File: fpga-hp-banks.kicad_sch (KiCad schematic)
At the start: 9 parts, among them U34 XCAU25P-2FFVB676I

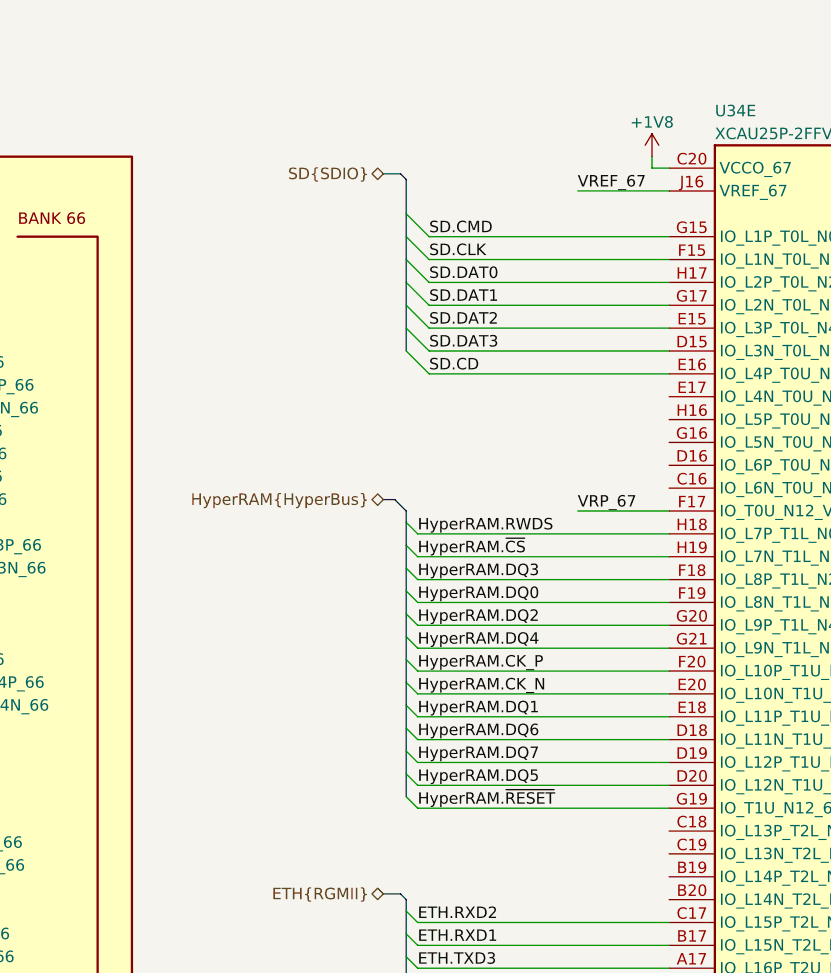
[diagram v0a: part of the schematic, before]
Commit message: [#67016] Remap HyperRAM interface
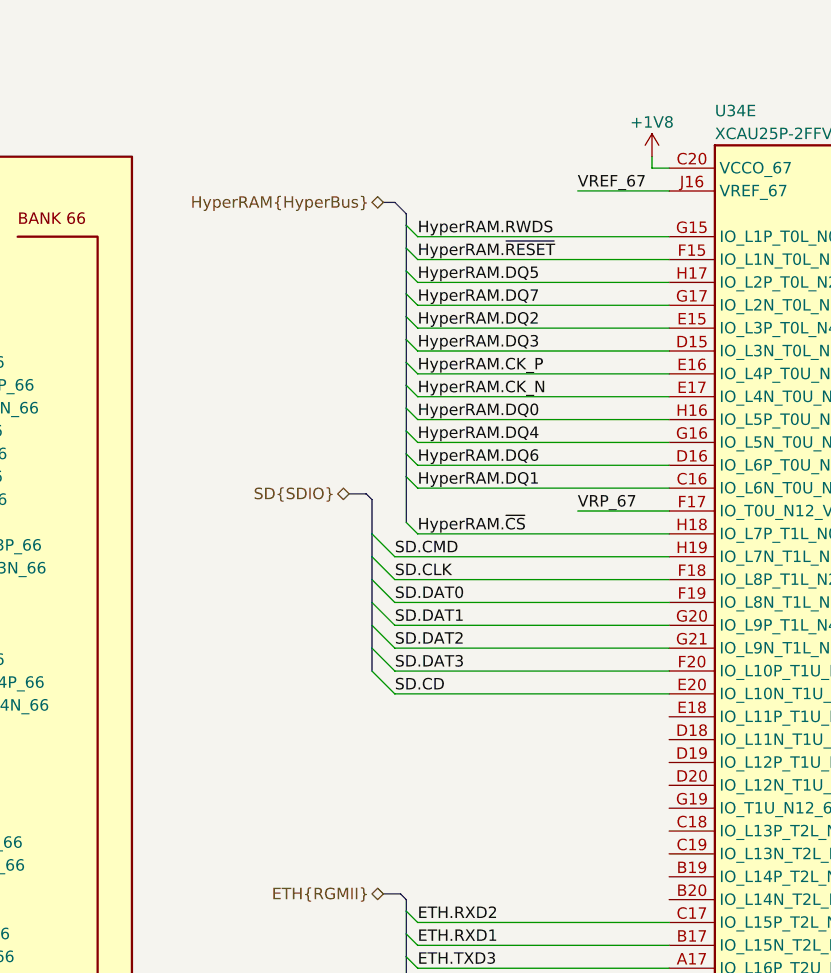
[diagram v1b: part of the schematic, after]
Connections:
- net HyperRAM.CK_N: now also U34.E17 (IO_L4N_T0U_N7_DBC_AD7N_67); no longer U34.E20 (IO_L10N_T1U_N7_QBC_AD4N_67)
- net HyperRAM.CK_P: now also U34.E16 (IO_L4P_T0U_N6_DBC_AD7P_67); no longer U34.F20 (IO_L10P_T1U_N6_QBC_AD4P_67)
- net HyperRAM.DQ0: now also U34.H16 (IO_L5P_T0U_N8_AD14P_67); no longer U34.F19 (IO_L8N_T1L_N3_AD5N_67)
- net HyperRAM.DQ1: now also U34.C16 (IO_L6N_T0U_N11_AD6N_67); no longer U34.E18 (IO_L11P_T1U_N8_GC_67)
- net HyperRAM.DQ2: now also U34.E15 (IO_L3P_T0L_N4_AD15P_67); no longer U34.G20 (IO_L9P_T1L_N4_AD12P_67)
- net HyperRAM.DQ3: now also U34.D15 (IO_L3N_T0L_N5_AD15N_67); no longer U34.F18 (IO_L8P_T1L_N2_AD5P_67)
- net HyperRAM.DQ4: now also U34.G16 (IO_L5N_T0U_N9_AD14N_67); no longer U34.G21 (IO_L9N_T1L_N5_AD12N_67)
- net HyperRAM.DQ5: now also U34.H17 (IO_L2P_T0L_N2_67); no longer U34.D20 (IO_L12N_T1U_N11_GC_67)
- net HyperRAM.DQ6: now also U34.D16 (IO_L6P_T0U_N10_AD6P_67); no longer U34.D18 (IO_L11N_T1U_N9_GC_67)
- net HyperRAM.DQ7: now also U34.G17 (IO_L2N_T0L_N3_67); no longer U34.D19 (IO_L12P_T1U_N10_GC_67)
- net HyperRAM.RWDS: now also U34.G15 (IO_L1P_T0L_N0_DBC_67); no longer U34.H18 (IO_L7P_T1L_N0_QBC_AD13P_67)
- net HyperRAM.~{CS}: now also U34.H18 (IO_L7P_T1L_N0_QBC_AD13P_67); no longer U34.H19 (IO_L7N_T1L_N1_QBC_AD13N_67)
- net HyperRAM.~{RESET}: now also U34.F15 (IO_L1N_T0L_N1_DBC_67); no longer U34.G19 (IO_T1U_N12_67)
- net SD.CD: now also U34.E20 (IO_L10N_T1U_N7_QBC_AD4N_67); no longer U34.E16 (IO_L4P_T0U_N6_DBC_AD7P_67)
- net SD.CLK: now also U34.F18 (IO_L8P_T1L_N2_AD5P_67); no longer U34.F15 (IO_L1N_T0L_N1_DBC_67)
- net SD.CMD: now also U34.H19 (IO_L7N_T1L_N1_QBC_AD13N_67); no longer U34.G15 (IO_L1P_T0L_N0_DBC_67)
- net SD.DAT0: now also U34.F19 (IO_L8N_T1L_N3_AD5N_67); no longer U34.H17 (IO_L2P_T0L_N2_67)
- net SD.DAT1: now also U34.G20 (IO_L9P_T1L_N4_AD12P_67); no longer U34.G17 (IO_L2N_T0L_N3_67)
- net SD.DAT2: now also U34.G21 (IO_L9N_T1L_N5_AD12N_67); no longer U34.E15 (IO_L3P_T0L_N4_AD15P_67)
- net SD.DAT3: now also U34.F20 (IO_L10P_T1U_N6_QBC_AD4P_67); no longer U34.D15 (IO_L3N_T0L_N5_AD15N_67)

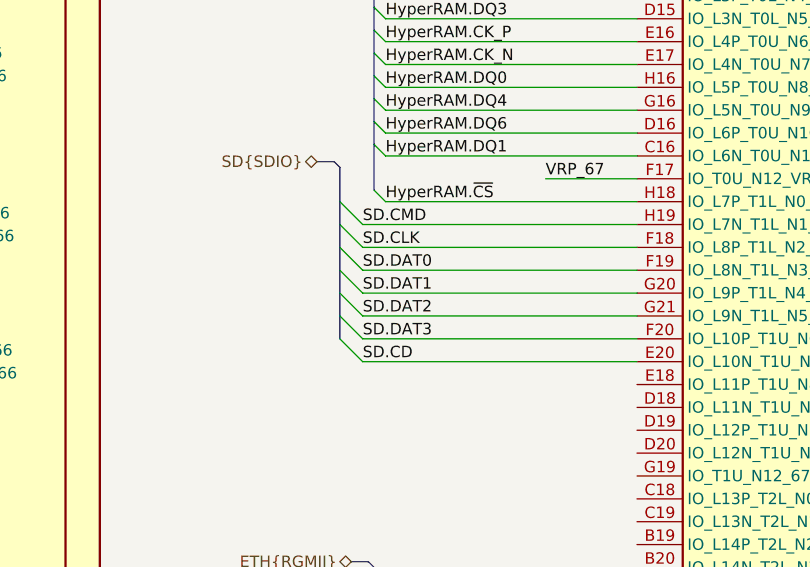
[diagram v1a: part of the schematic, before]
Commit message: [#67016] Connect SD card
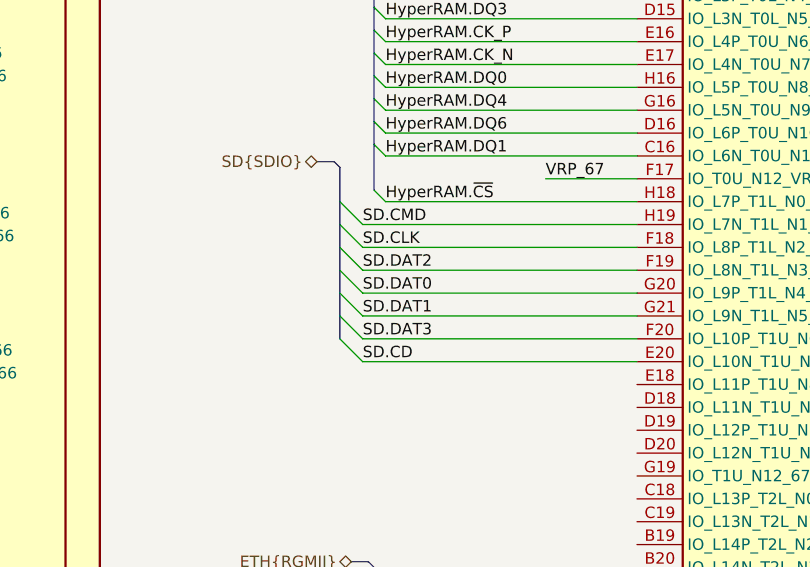
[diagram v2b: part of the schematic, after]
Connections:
- net SD.DAT0: now also U34.G20 (IO_L9P_T1L_N4_AD12P_67); no longer U34.F19 (IO_L8N_T1L_N3_AD5N_67)
- net SD.DAT1: now also U34.G21 (IO_L9N_T1L_N5_AD12N_67); no longer U34.G20 (IO_L9P_T1L_N4_AD12P_67)
- net SD.DAT2: now also U34.F19 (IO_L8N_T1L_N3_AD5N_67); no longer U34.G21 (IO_L9N_T1L_N5_AD12N_67)
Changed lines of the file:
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@@
     (effects (font (size 1.27 1.27)) (justify left bottom))
   )
-  (label "SD.DAT2" (at 311.15 104.14 0) (fields_autoplaced)
+  (label "SD.DAT2" (at 311.15 99.06 0) (fields_autoplaced)
     (effects (font (size 1.27 1.27)) (justify left bottom))
   )
@@
     (effects (font (size 1.27 1.27)) (justify left bottom))
   )
-  (label "SD.DAT1" (at 311.15 101.6 0) (fields_autoplaced)
+  (label "SD.DAT1" (at 311.15 104.14 0) (fields_autoplaced)
     (effects (font (size 1.27 1.27)) (justify left bottom))
   )
@@
     (effects (font (size 1.27 1.27)) (justify left bottom))
   )
-  (label "SD.DAT0" (at 311.15 99.06 0) (fields_autoplaced)
-    (effects (font (size 1.27 1.27)) (justify left bottom))
-  )
+  (label "SD.DAT0" (at 311.15 101.6 0) (fields_autoplaced)
+    (effects (font (size 1.27 1.27)) (justify left bottom))
+  )

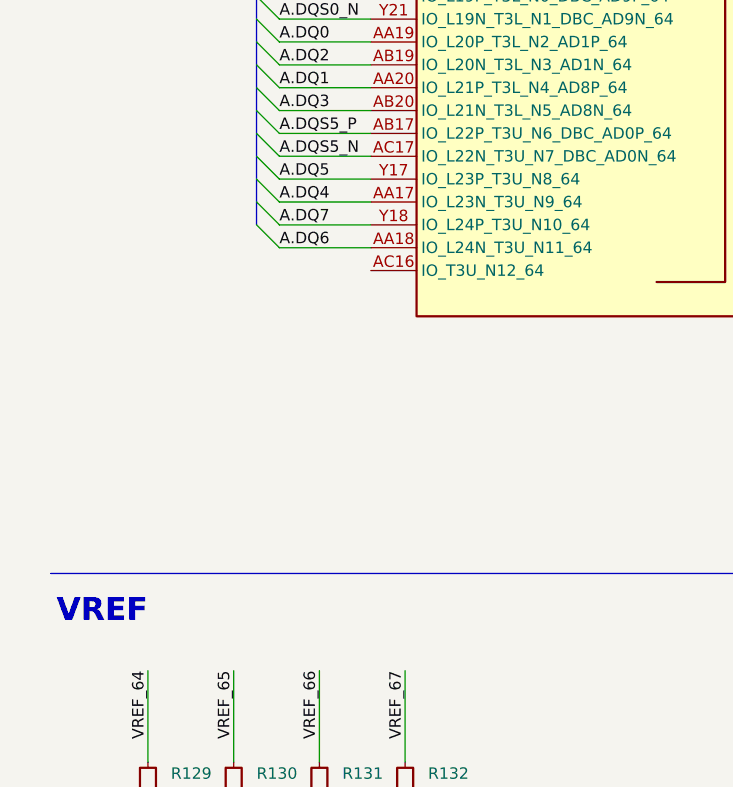
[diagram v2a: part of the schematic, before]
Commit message: [#67115] Place decoupling under FPGA
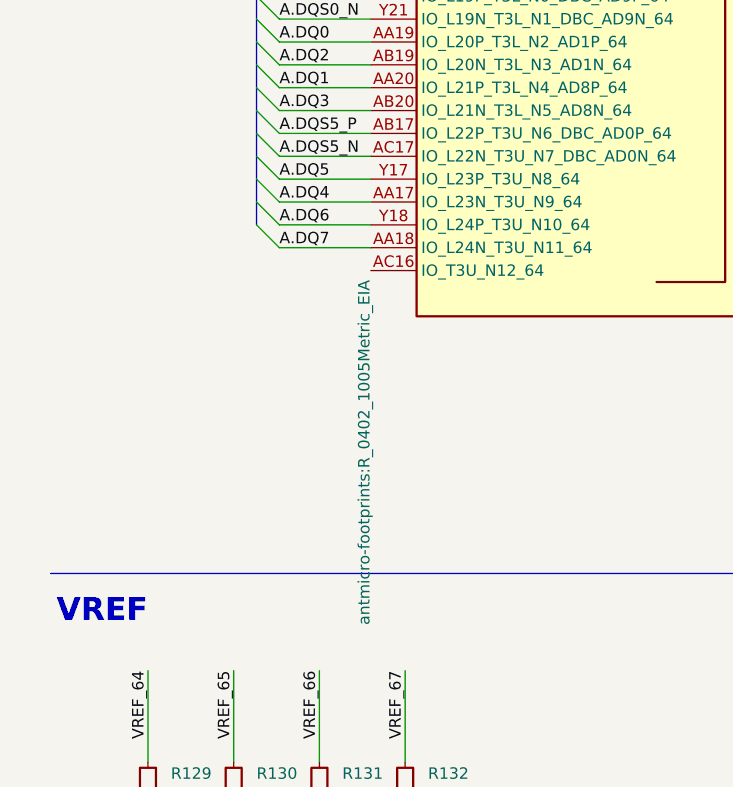
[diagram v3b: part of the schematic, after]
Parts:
- R129, R130, R131, R132, R133, R134, R180, R182: footprint antmicro-footprints:R_0402_1005Metric -> antmicro-footprints:R_0402_1005Metric_EIA
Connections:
- net A.DQ6: now also U34.Y18 (IO_L24P_T3U_N10_64); no longer U34.AA18 (IO_L24N_T3U_N11_64)
- net A.DQ7: now also U34.AA18 (IO_L24N_T3U_N11_64); no longer U34.Y18 (IO_L24P_T3U_N10_64)
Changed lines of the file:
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@@
     (effects (font (size 1.27 1.27)) (justify left bottom))
   )
-  (label "A.DQ6" (at 38.1 185.42 0) (fields_autoplaced)
+  (label "A.DQ6" (at 38.1 182.88 0) (fields_autoplaced)
     (effects (font (size 1.27 1.27)) (justify left bottom))
   )
@@
     (effects (font (size 1.27 1.27)) (justify left bottom))
   )
-  (label "A.DQ7" (at 38.1 182.88 0) (fields_autoplaced)
+  (label "A.DQ7" (at 38.1 185.42 0) (fields_autoplaced)
     (effects (font (size 1.27 1.27)) (justify left bottom))
   )
@@
       (effects (font (size 1.27 1.27) (thickness 0.15)) (justify left bottom) hide)
     )
-    (property "Footprint" "antmicro-footprints:R_0402_1005Metric" (at 57.785 227.33 0)
+    (property "Footprint" "antmicro-footprints:R_0402_1005Metric_EIA" (at 57.785 227.33 0)
       (effects (font (size 1.27 1.27) (thickness 0.15)) (justify left bottom) hide)
     )
@@
       (effects (font (size 1.27 1.27) (thickness 0.15)) (justify left bottom) hide)
     )
-    (property "Footprint" "antmicro-footprints:R_0402_1005Metric" (at 151.765 269.24 0)
+    (property "Footprint" "antmicro-footprints:R_0402_1005Metric_EIA" (at 151.765 269.24 0)
       (effects (font (size 1.27 1.27) (thickness 0.15)) (justify left bottom) hide)
     )
@@
       (effects (font (size 1.27 1.27) (thickness 0.15)) (justify left bottom) hide)
     )
-    (property "Footprint" "antmicro-footprints:R_0402_1005Metric" (at 210.82 269.24 0)
+    (property "Footprint" "antmicro-footprints:R_0402_1005Metric_EIA" (at 210.82 269.24 0)
       (effects (font (size 1.27 1.27) (thickness 0.15)) (justify left bottom) hide)
     )
@@
       (effects (font (size 1.27 1.27) (thickness 0.15)) (justify left bottom) hide)
     )
-    (property "Footprint" "antmicro-footprints:R_0402_1005Metric" (at 172.72 269.24 0)
+    (property "Footprint" "antmicro-footprints:R_0402_1005Metric_EIA" (at 172.72 269.24 0)
       (effects (font (size 1.27 1.27) (thickness 0.15)) (justify left bottom) hide)
     )
@@
       (effects (font (size 1.27 1.27) (thickness 0.15)) (justify left bottom) hide)
     )
-    (property "Footprint" "antmicro-footprints:R_0402_1005Metric" (at 48.26 227.33 0)
-      (effects (font (size 1.27 1.27) (thickness 0.15)) (justify left bottom) hide)
+    (property "Footprint" "antmicro-footprints:R_0402_1005Metric_EIA" (at 48.26 227.33 0)
+      (effects (font (size 1.27 1.27) (thickness 0.15)) (justify left bottom))
     )
     (property "Datasheet" "https://www.bourns.com/docs/product-datasheets/cr.pdf" (at 50.8 227.33 0)
@@
       (effects (font (size 1.27 1.27) (thickness 0.15)) (justify left bottom) hide)
     )
-    (property "Footprint" "antmicro-footprints:R_0402_1005Metric" (at 191.77 269.24 0)
+    (property "Footprint" "antmicro-footprints:R_0402_1005Metric_EIA" (at 191.77 269.24 0)
       (effects (font (size 1.27 1.27) (thickness 0.15)) (justify left bottom) hide)
     )
@@
       (effects (font (size 1.27 1.27) (thickness 0.15)) (justify left bottom) hide)
     )
-    (property "Footprint" "antmicro-footprints:R_0402_1005Metric" (at 38.735 227.33 0)
+    (property "Footprint" "antmicro-footprints:R_0402_1005Metric_EIA" (at 38.735 227.33 0)
       (effects (font (size 1.27 1.27) (thickness 0.15)) (justify left bottom) hide)
     )
@@
       (effects (font (size 1.27 1.27) (thickness 0.15)) (justify left bottom) hide)
     )
-    (property "Footprint" "antmicro-footprints:R_0402_1005Metric" (at 67.31 227.33 0)
+    (property "Footprint" "antmicro-footprints:R_0402_1005Metric_EIA" (at 67.31 227.33 0)
       (effects (font (size 1.27 1.27) (thickness 0.15)) (justify left bottom) hide)
     )

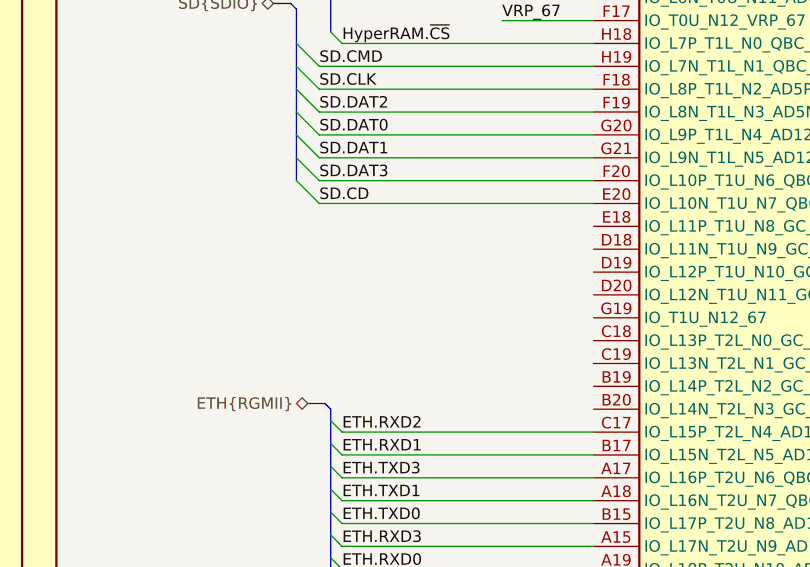
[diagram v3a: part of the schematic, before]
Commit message: [#66312] Started connecting SI5319C-C-GM-ND
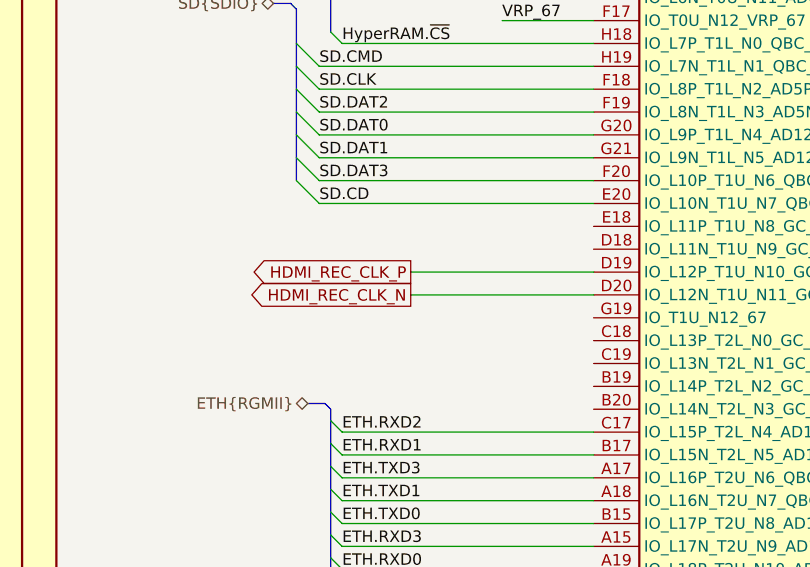
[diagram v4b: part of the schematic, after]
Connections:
- net HDMI_REC_CLK_P: now reaches U34.D19 (IO_L12P_T1U_N10_GC_67)
- net HDMI_REC_CLK_N: now reaches U34.D20 (IO_L12N_T1U_N11_GC_67)
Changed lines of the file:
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@@
     (stroke (width 0) (type default))
   )
+  (wire (pts (xy 321.31 119.38) (xy 341.63 119.38))
+    (stroke (width 0) (type default))
+  )
   (wire (pts (xy 228.6 171.45) (xy 238.76 171.45))
     (stroke (width 0) (type default))
@@
     (stroke (width 0) (type default))
   )
+  (wire (pts (xy 321.31 116.84) (xy 341.63 116.84))
+    (stroke (width 0) (type default))
+  )
   (bus (pts (xy 226.06 72.39) (xy 226.06 74.93))
     (stroke (width 0) (type default))
@@
     (effects (font (size 1.27 1.27)) (justify left bottom))
   )
+  (global_label "HDMI_REC_CLK_N" (shape output) (at 321.31 119.38 180) (fields_autoplaced)
+    (effects (font (size 1.27 1.27)) (justify right))
+    (property "Intersheetrefs" "${INTERSHEET_REFS}" (at 302.8319 119.38 0)
+      (effects (font (size 1.27 1.27)) (justify right))
+    )
+  )
+  (global_label "HDMI_REC_CLK_P" (shape output) (at 321.31 116.84 180) (fields_autoplaced)
+    (effects (font (size 1.27 1.27)) (justify right))
+    (property "Intersheetrefs" "${INTERSHEET_REFS}" (at 302.8924 116.84 0)
+      (effects (font (size 1.27 1.27)) (justify right))
+    )
+  )
   (hierarchical_label "SD{SDIO}" (shape bidirectional) (at 306.07 86.995 180) (fields_autoplaced)
